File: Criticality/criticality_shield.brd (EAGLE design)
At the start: 100 x 80 mm, 20 parts

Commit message: some small improvements
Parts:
- renumbered SV2 to D8-13
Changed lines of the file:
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@@
 <attribute name="OC_FARNELL" value="unknown" x="59" y="74" size="1.778" layer="27" rot="R180" display="off"/>
 </element>
-<element name="SV2" library="con-lstb" package="MA08-1" value="" x="37" y="74" rot="R180">
+<element name="D8-13" library="con-lstb" package="MA08-1" value="" x="37" y="74" rot="R180">
 <attribute name="OC_NEWARK" value="unknown" x="37" y="74" size="1.778" layer="27" rot="R180" display="off"/>
 <attribute name="MPN" value="" x="37" y="74" size="1.778" layer="27" rot="R180" display="off"/>
@@
 <signal name="N$19">
 <contactref element="R9" pad="1"/>
-<contactref element="SV2" pad="3"/>
+<contactref element="D8-13" pad="3"/>
 <wire x1="31" y1="69.4" x2="40.81" y2="74" width="0" layer="19" extent="1-1"/>
 </signal>
 <signal name="N$20">
 <contactref element="R10" pad="1"/>
-<contactref element="SV2" pad="4"/>
+<contactref element="D8-13" pad="4"/>
 <wire x1="28" y1="69.4" x2="38.27" y2="74" width="0" layer="19" extent="1-1"/>
 </signal>
 <signal name="N$21">
 <contactref element="R11" pad="1"/>
-<contactref element="SV2" pad="5"/>
+<contactref element="D8-13" pad="5"/>
 <wire x1="25" y1="69.4" x2="35.73" y2="74" width="0" layer="19" extent="1-1"/>
 </signal>
 <signal name="N$22">
 <contactref element="R12" pad="1"/>
-<contactref element="SV2" pad="6"/>
+<contactref element="D8-13" pad="6"/>
 <wire x1="22" y1="69.4" x2="33.19" y2="74" width="0" layer="19" extent="1-1"/>
 </signal>
 <signal name="N$23">
 <contactref element="R13" pad="1"/>
-<contactref element="SV2" pad="7"/>
+<contactref element="D8-13" pad="7"/>
 <wire x1="19" y1="69.4" x2="30.65" y2="74" width="0" layer="19" extent="1-1"/>
 </signal>
 <signal name="N$15">
-<contactref element="SV2" pad="1"/>
+<contactref element="D8-13" pad="1"/>
 <contactref element="R7" pad="1"/>
 <wire x1="37" y1="69.4" x2="45.89" y2="74" width="0" layer="19" extent="1-1"/>
 </signal>
 <signal name="N$16">
-<contactref element="SV2" pad="2"/>
+<contactref element="D8-13" pad="2"/>
 <contactref element="R8" pad="1"/>
 <wire x1="34" y1="69.4" x2="43.35" y2="74" width="0" layer="19" extent="1-1"/>
 </signal>
 <signal name="N$17">
-<contactref element="SV2" pad="8"/>
+<contactref element="D8-13" pad="8"/>
 <contactref element="R14" pad="1"/>
 <wire x1="16" y1="69.4" x2="28.11" y2="74" width="0" layer="19" extent="1-1"/>

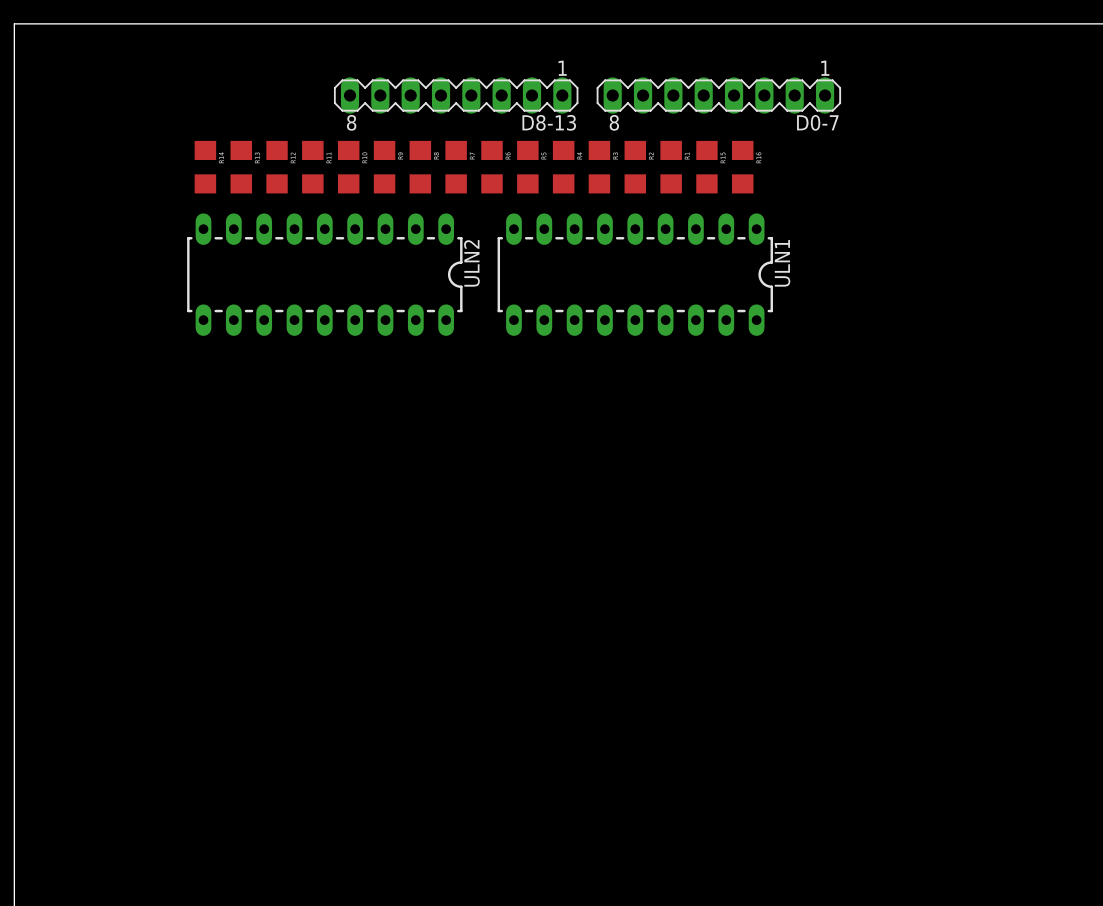
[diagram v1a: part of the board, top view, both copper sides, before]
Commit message: added layers to "criticality"
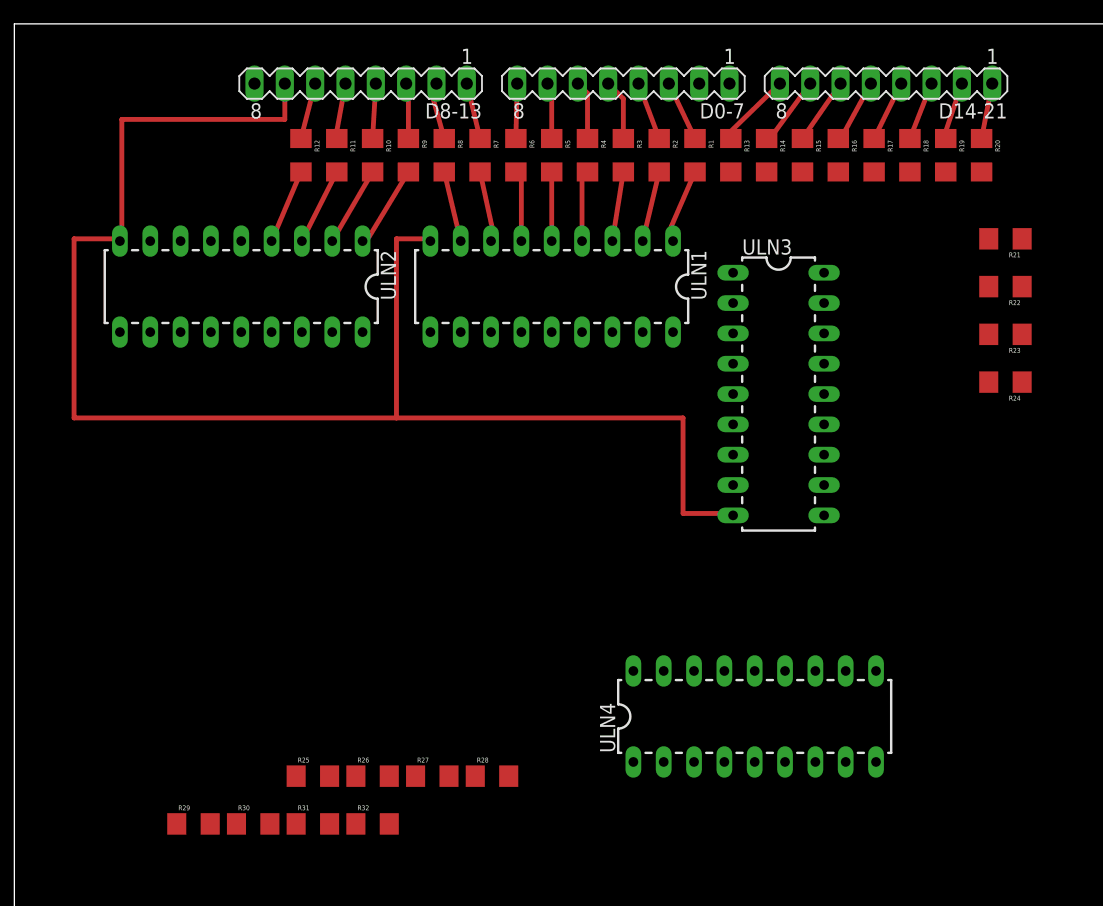
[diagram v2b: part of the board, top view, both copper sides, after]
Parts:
- added D14-21: (no value), con-lstb:MA08-1
- added R17, R18, R19, R20, R21, R22, R23, R24, R25, R26, R27, R28, R29, R30, R31, R32: 100, SparkFun-Passives:1206
- added ULN3, ULN4: ULN2803, SparkFun-PowerIC:DIL18
- moved R14 47.0 mm to (63.0, 69.0)
- moved R13 41.0 mm to (60.0, 69.0)
- moved D0-7 8.06 mm to (51.0, 75.0)
- moved D8-13 8.06 mm to (29.0, 75.0)
- moved R15 8.06 mm to (66.0, 69.0)
- moved R16 8.06 mm to (69.0, 69.0)
- moved ULN1 7.07 mm to (45.0, 58.0)
- moved ULN2 7.07 mm to (19.0, 58.0)
- moved R1 2.24 mm to (57.0, 69.0)
- moved R10 2.24 mm to (30.0, 69.0)
- moved R11 2.24 mm to (27.0, 69.0)
- moved R12 2.24 mm to (24.0, 69.0)
- moved R2 2.24 mm to (54.0, 69.0)
- moved R3 2.24 mm to (51.0, 69.0)
- moved R4 2.24 mm to (48.0, 69.0)
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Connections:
- new net N$31: D14-21.6, R15.1
- new net N$32: D14-21.5, R16.1
- new net N$33: R21.2, ULN3.5
- new net N$34: R22.2, ULN3.6
- new net N$35: R23.2, ULN3.7
- new net N$36: R24.2, ULN3.8
- new net N$37: D14-21.7, R14.1
- new net N$38: D14-21.2, R19.1
- new net N$39: D14-21.1, R20.1
- new net N$40: D14-21.3, R18.1
- new net N$43: R18.2, ULN3.2
- new net N$44: R19.2, ULN3.3
- new net N$45: R20.2, ULN3.4
- new net N$46: R17.2, ULN3.1
- new net N$53: R25.2, ULN4.1
- new net N$54: R26.2, ULN4.2
- new net N$55: R27.2, ULN4.3
- new net N$56: R28.2, ULN4.4
- new net N$57: R29.2, ULN4.5
- new net N$58: R30.2, ULN4.6
- new net N$59: R31.2, ULN4.7
- new net N$60: R32.2, ULN4.8
- net GND: now also D8-13.7, ULN3.9, ULN4.9
- net N$17: now also D14-21.8, R13.1; no longer D8-13.8, R14.1
- net N$23: now also D14-21.4, R17.1; no longer D8-13.7, R13.1
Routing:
- net GND: track 0.00 -> 127.0 mm
- net N$18: track 0.00 -> 8.54 mm
- net N$24: track 0.00 -> 6.70 mm
- net N$37: track 0.00 -> 6.59 mm
- net N$25: track 0.00 -> 6.48 mm
- net N$17: track 0.00 -> 6.34 mm
- net N$26: track 0.00 -> 6.29 mm
- net N$10: track 0.00 -> 6.22 mm
- net N$32: track 0.00 -> 6.10 mm
- net N$9: track 0.00 -> 5.98 mm
- net N$12: track 0.00 -> 5.98 mm
- net N$7: track 0.00 -> 5.95 mm
- net N$14: track 0.00 -> 5.95 mm
- net N$13: track 0.00 -> 5.90 mm
- net N$8: track 0.00 -> 5.86 mm
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
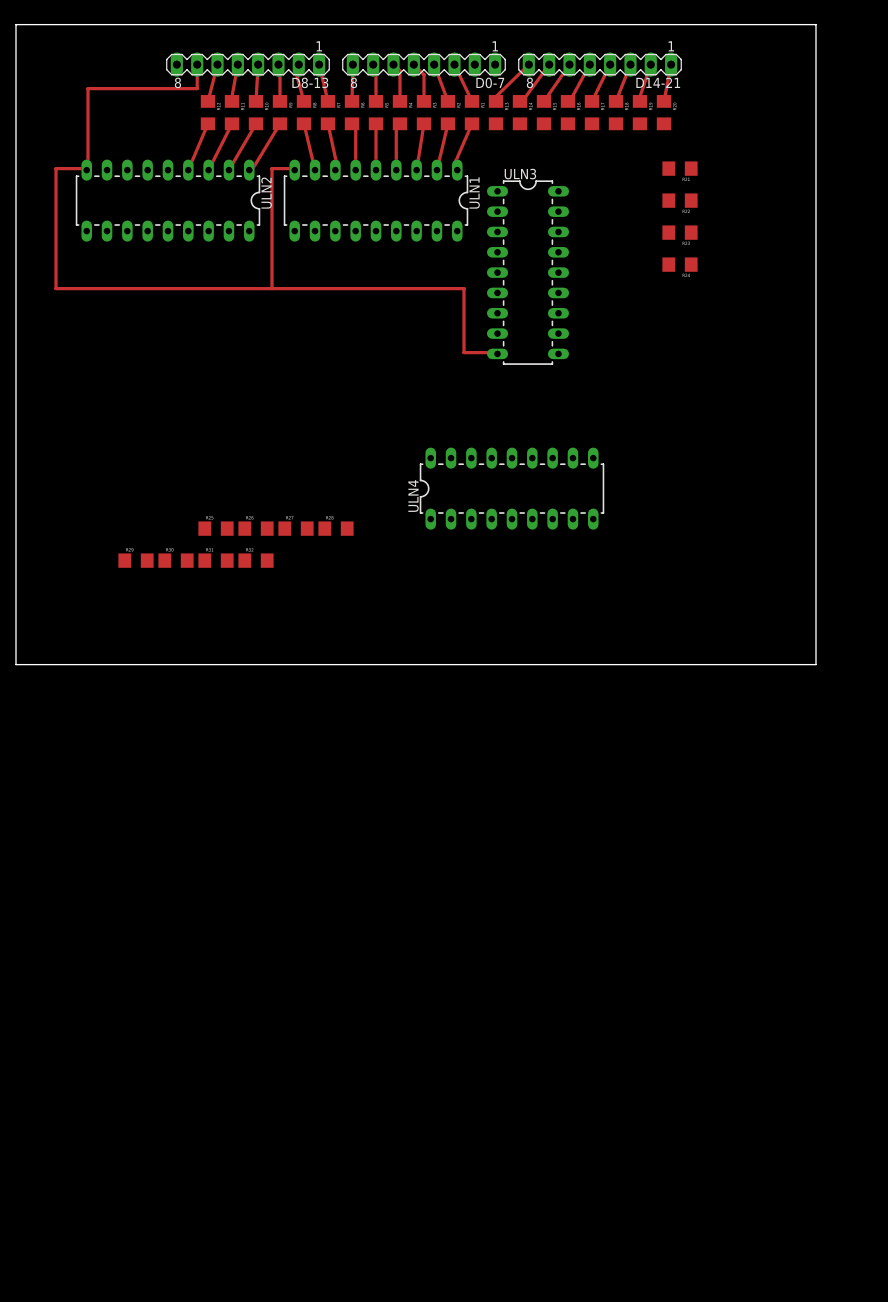
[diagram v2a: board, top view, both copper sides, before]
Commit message: rearranged, all parts connected
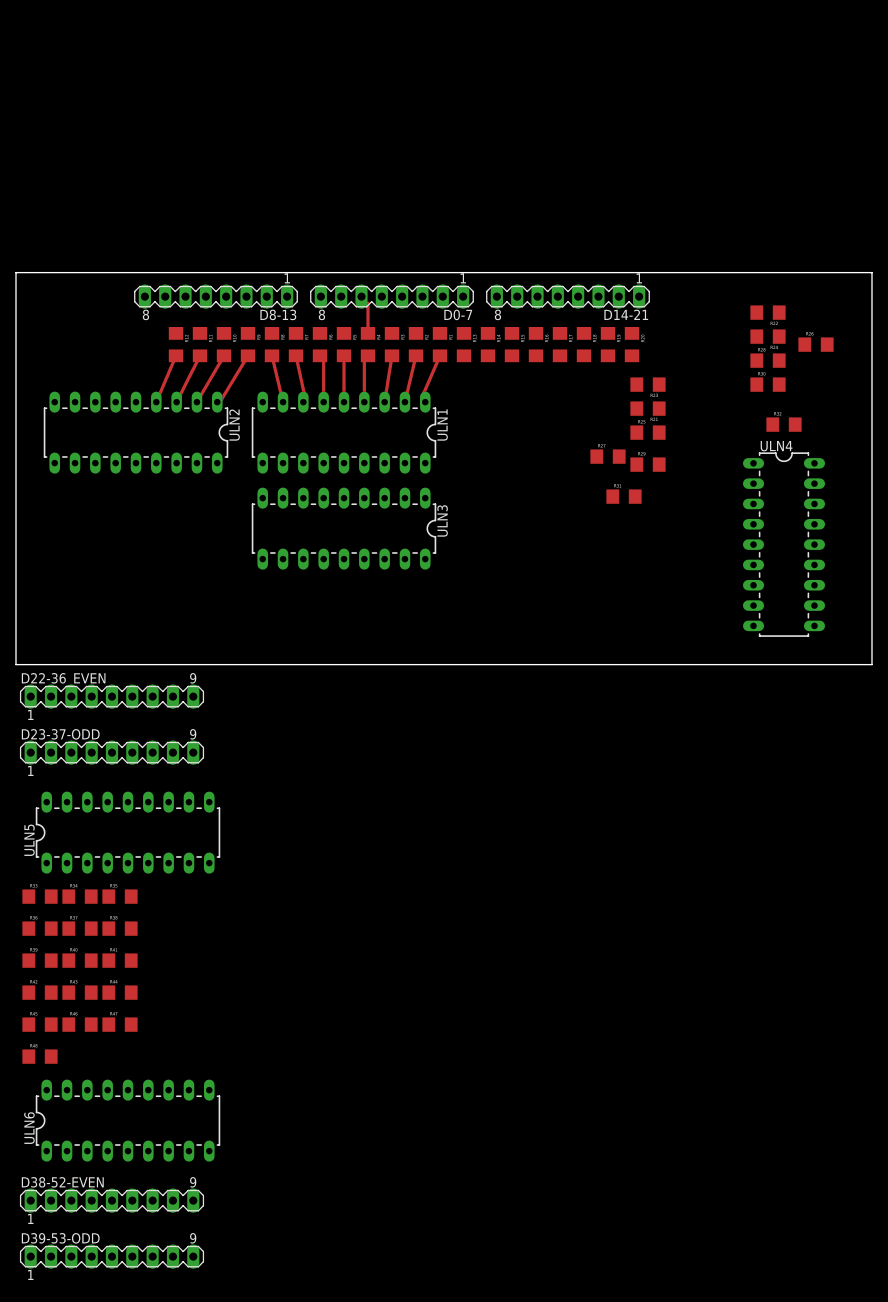
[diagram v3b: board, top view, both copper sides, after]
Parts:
- added D22-36_EVEN, D23-37-ODD, D38-52-EVEN, D39-53-ODD: (no value), con-lstb:MA09-1
- added R33, R34, R35, R36, R37, R38, R39, R40, R41, R42, R43, R44, R45, R46, R47, R48: 100, SparkFun-Passives:1206
- added ULN5, ULN6: ULN2803, SparkFun-PowerIC:DIL18
- moved R30 77.2 mm to (94.0, 35.0)
- moved R26 73.7 mm to (100.0, 40.0)
- moved R32 68.2 mm to (96.0, 30.0)
- moved R29 65.1 mm to (79.0, 25.0)
- moved R28 57.9 mm to (94.0, 38.0)
- moved R25 55.3 mm to (79.0, 29.0)
- moved R31 51.6 mm to (76.0, 21.0)
- moved R27 40.0 mm to (74.0, 26.0)
- moved ULN3 39.4 mm to (41.0, 17.0), turned to 180 degrees
- moved ULN4 34.7 mm to (96.0, 15.0), turned to 270 degrees
- moved R21 30.3 mm to (79.0, 32.0)
- moved D0-7 29.3 mm to (47.0, 46.0)
- moved D14-21 29.3 mm to (69.0, 46.0)
- moved D8-13 29.3 mm to (25.0, 46.0)
- moved R1 29.3 mm to (53.0, 40.0)
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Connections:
- removed net N$17 (its old number): D14-21.8, R13.1
- new net +5V: D22-36_EVEN.9, D23-37-ODD.9, ULN1.10, ULN2.10, ULN3.10, ULN4.10, ULN5.10, ULN6.10
- new net N$20: D14-21.1, R13.1
- new net N$21: D14-21.2, R14.1
- new net N$22: D14-21.3, R15.1
- new net N$41: D22-36_EVEN.6, R23.1
- new net N$42: D22-36_EVEN.5, R24.1
- new net N$47: D22-36_EVEN.4, R25.1
- new net N$48: D22-36_EVEN.3, R26.1
- new net N$49: D22-36_EVEN.2, R27.1
- new net N$50: D22-36_EVEN.1, R28.1
- new net N$51: D23-37-ODD.8, R29.1
- new net N$52: D23-37-ODD.7, R30.1
- new net N$61: D23-37-ODD.6, R31.1
- new net N$62: D23-37-ODD.5, R32.1
- new net N$63: D23-37-ODD.4, R33.1
- new net N$64: R33.2, ULN5.1
- new net N$65: R34.2, ULN5.2
- new net N$68: R35.2, ULN5.3
- new net N$69: R36.2, ULN5.4
- new net N$70: R37.2, ULN5.5
- new net N$71: R38.2, ULN5.6
- new net N$72: R39.2, ULN5.7
- new net N$73: R40.2, ULN5.8
- new net N$74: R41.2, ULN6.1
- new net N$75: R42.2, ULN6.2
- new net N$76: R43.2, ULN6.3
- new net N$77: R44.2, ULN6.4
- new net N$78: R45.2, ULN6.5
- new net N$79: R46.2, ULN6.6
- new net N$80: R47.2, ULN6.7
- new net N$81: R48.2, ULN6.8
- new net N$82: D23-37-ODD.3, R34.1
- new net N$83: D23-37-ODD.2, R35.1
- new net N$84: D23-37-ODD.1, R36.1
- new net N$85: D38-52-EVEN.9, R37.1
- new net N$86: D38-52-EVEN.8, R38.1
- new net N$87: D38-52-EVEN.7, R39.1
- new net N$88: D38-52-EVEN.6, R40.1
- new net N$89: D38-52-EVEN.5, R41.1
- new net N$90: D38-52-EVEN.4, R42.1
- new net N$91: D38-52-EVEN.3, R43.1
- new net N$92: D38-52-EVEN.2, R44.1
- new net N$93: D39-53-ODD.9, R45.1
- new net N$94: D39-53-ODD.8, R46.1
- new net N$95: D39-53-ODD.7, R47.1
- new net N$96: D39-53-ODD.6, R48.1
- net GND: now also D38-52-EVEN.1, D39-53-ODD.1, ULN5.9, ULN6.9
- net N$23: now also R16.1; no longer R17.1
- net N$31: now also D14-21.5, R17.1; no longer D14-21.6, R15.1
- net N$32: now also D14-21.6, R18.1; no longer D14-21.5, R16.1
- net N$37: now also R19.1; no longer R14.1
- net N$38: now also D14-21.8, R20.1; no longer D14-21.2, R19.1
- net N$39: now also D22-36_EVEN.8, R21.1; no longer D14-21.1, R20.1
- net N$40: now also D22-36_EVEN.7, R22.1; no longer D14-21.3, R18.1
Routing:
- net GND: track 127.0 -> 0.00 mm
- net N$37: track 6.59 -> 0.00 mm
- net N$17 (its old number): track 6.34 -> 0.00 mm
- net N$32: track 6.10 -> 0.00 mm
- net N$31: track 5.60 -> 0.00 mm
- net N$23: track 5.13 -> 0.00 mm
- net N$1: track 5.09 -> 0.00 mm
- net N$15: track 5.08 -> 0.00 mm
- net N$40: track 4.94 -> 0.00 mm
- net N$67: track 4.91 -> 0.00 mm
- net N$6: track 4.88 -> 0.00 mm
- net N$38: track 4.82 -> 0.00 mm
- net N$19: track 4.75 -> 0.00 mm
- net N$2: track 4.74 -> 0.00 mm
- net N$5: track 4.73 -> 0.00 mm
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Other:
- board size 100 x 80 mm -> 107 x 49 mm

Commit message: wired up everything, too messy..
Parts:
- moved D39-53-ODD 119.0 mm to (85.0, 20.0), turned to 270 degrees
- moved D38-52-EVEN 111.7 mm to (82.0, 20.0), turned to 270 degrees
- moved ULN6 93.6 mm to (61.0, 24.0)
- moved D23-37-ODD 90.8 mm to (85.0, 43.0), turned to 270 degrees
- moved R33 85.6 mm to (66.0, 29.0)
- moved R34 85.6 mm to (71.0, 29.0)
- moved R35 85.6 mm to (76.0, 29.0)
- moved R36 85.6 mm to (66.0, 25.0)
- moved R37 85.6 mm to (71.0, 25.0)
- moved R38 85.6 mm to (76.0, 25.0)
- moved R39 85.6 mm to (66.0, 21.0)
- moved R40 85.6 mm to (71.0, 21.0)
- moved R41 85.6 mm to (76.0, 21.0)
- moved R42 85.6 mm to (66.0, 17.0)
- moved R43 85.6 mm to (71.0, 17.0)
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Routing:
- net N$18: track 8.54 -> 0.00 mm
- net N$24: track 6.70 -> 0.00 mm
- net N$25: track 6.48 -> 0.00 mm
- net N$26: track 6.29 -> 0.00 mm
- net N$10: track 6.22 -> 0.00 mm
- net N$9: track 5.98 -> 0.00 mm
- net N$12: track 5.98 -> 0.00 mm
- net N$7: track 5.95 -> 0.00 mm
- net N$14: track 5.95 -> 0.00 mm
- net N$13: track 5.90 -> 0.00 mm
- net N$8: track 5.86 -> 0.00 mm
- net N$11: track 5.79 -> 0.00 mm
- net N$4: track 3.79 -> 0.00 mm
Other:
- board size 107 x 49 mm -> 99 x 80 mm
